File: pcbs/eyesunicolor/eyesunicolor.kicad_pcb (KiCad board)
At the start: 2 copper layers, 209.3 x 100.6 mm, 45 parts, among them J1 SUPP28, J2 SUPP28, P1 CONN_5X2, P2 CONN_5X2, P3 CONN_5X2

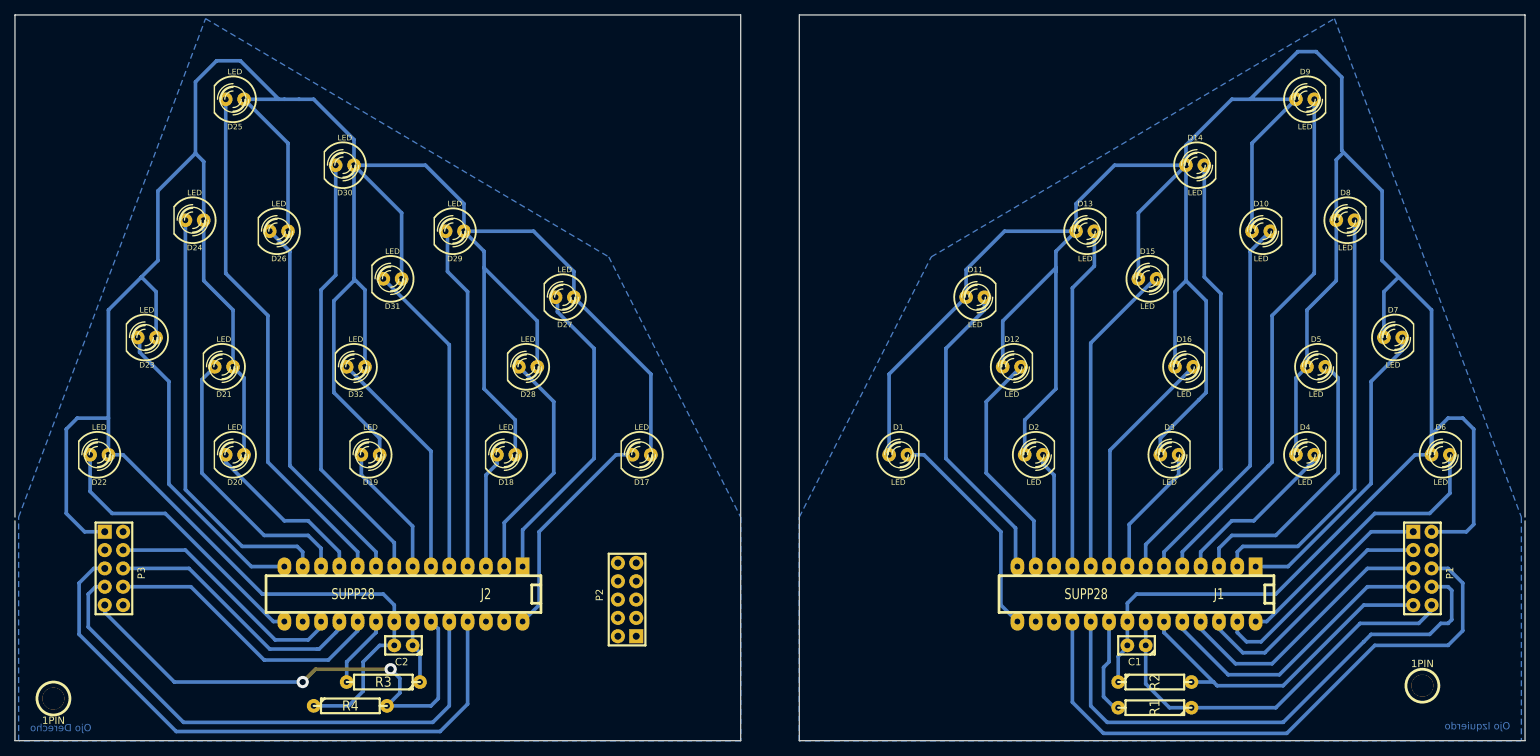
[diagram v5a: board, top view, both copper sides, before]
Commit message: Elimino archivos de backup y actualizo pcb y schm
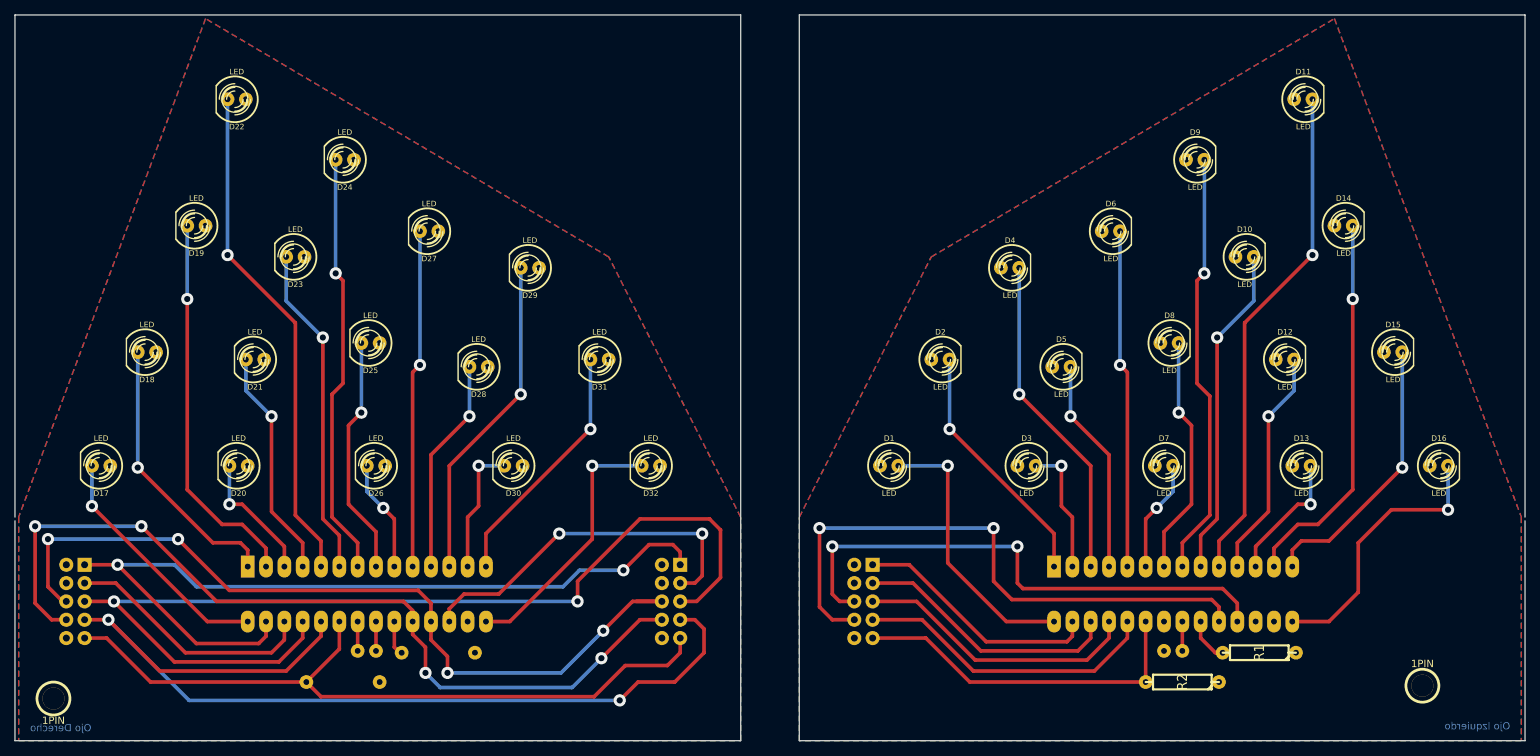
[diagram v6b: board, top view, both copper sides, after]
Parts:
- C1, C2: value C -> 100n; moved to B.Cu
- J1, J2, P1, P2, P3, R3, R4: moved to B.Cu
- moved P1 77.6 mm to (297.4, 109.7)
- moved P3 77.4 mm to (270.8, 109.7)
- moved P2 76.5 mm to (188.2, 109.7), turned to 270 degrees
- moved D17 74.9 mm to (191.8, 90.9)
- moved D6 55.2 mm to (331.7, 58.4)
- moved D11 53.1 mm to (358.4, 40.1)
- moved D22 52.8 mm to (210.6, 40.1)
- moved D18 51.8 mm to (198.1, 75.2)
- moved D4 48.4 mm to (317.8, 63.5)
- moved D30 47.8 mm to (248.9, 90.9)
- moved D13 44.2 mm to (358.1, 90.9)
- moved D32 43.1 mm to (268.0, 90.9)
- moved D19 39.9 mm to (205.0, 57.7)
- moved D25 38.7 mm to (229.1, 73.9)
- moved D16 37.9 mm to (377.2, 90.9)
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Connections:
- D1 pad 2: N-0000026 -> N-0000023
- D10 pad 2: N-0000037 -> N-0000035
- D14 pad 2: N-0000036 -> N-0000033
- D15 pad 2: N-0000025 -> N-0000026
- D19 pad 2: N-0000056 -> N-0000057
- D2 pad 2: N-0000033 -> N-0000040
- D22 pad 2: N-0000055 -> N-0000056
- D24 pad 2: N-0000057 -> N-0000052
- D25 pad 2: N-0000054 -> N-0000055
- D3 pad 2: N-0000035 -> N-0000039
- D5 pad 2: N-0000039 -> N-0000038
- D7 pad 2: N-0000040 -> N-0000037
- D9 pad 2: N-0000038 -> N-0000036
- J1 pad 10: N-0000025 -> N-0000027
- J1 pad 11: N-0000034 -> N-0000032
- J1 pad 12: N-0000033 -> N-0000034
- J1 pad 13: N-0000032 -> N-0000033
- J1 pad 14: N-0000027 -> N-0000026
- J1 pad 15: N-0000026 -> N-0000028
- J1 pad 16: (no net) -> N-0000025
- J1 pad 17: (no net) -> N-0000024
- J1 pad 2: N-0000030 -> N-0000039
- J1 pad 28: N-0000031 -> N-0000023
- J1 pad 3: N-0000039 -> N-0000029
- J1 pad 4: N-0000029 -> N-0000038
- J1 pad 5: N-0000038 -> N-0000031
- J1 pad 7: N-0000036 -> N-0000030
- J1 pad 8: N-0000035 -> N-0000036
- J1 pad 9: N-0000028 -> N-0000035
- J2 pad 1: N-0000046 -> N-0000047
- J2 pad 10: N-0000054 -> N-0000046
- J2 pad 11: N-0000050 -> N-0000044
- J2 pad 12: N-0000051 -> N-0000043
- J2 pad 13: N-0000057 -> N-0000014
- J2 pad 14: N-0000041 -> N-0000049
- J2 pad 15: N-0000055 -> N-0000048
- J2 pad 16: (no net) -> N-0000054
- J2 pad 2: N-0000044 -> N-0000057
- J2 pad 3: N-0000047 -> N-0000050
- J2 pad 4: N-0000043 -> N-0000051
- J2 pad 5: N-0000049 -> N-0000056
- J2 pad 6: N-0000048 -> N-0000041
- J2 pad 7: N-0000056 -> N-0000052
- J2 pad 8: N-0000014 -> N-0000055
- P1 pad 4: (no net) -> N-0000015
- P2 pad 2: /SCLK_D -> VCC
- P2 pad 4: (no net) -> N-000004
- P2 pad 5: /GSCLK_D -> /SCLK_D
- P2 pad 6: /XLAT_D -> /GSCLK_D
- P2 pad 7: VCC -> /XLAT_D
- P2 pad 8: /BLANK_D -> /DCPRG_D
- P2 pad 9: /DCPRG_D -> /BLANK_D
- P3 pad 1: VCC -> /VPRG_D
- P3 pad 2: (no net) -> VCC
- P3 pad 3: /VPRG_D -> /SOUT_D
- P3 pad 4: /SOUT_D -> N-0000011
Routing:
- net VCC: track 913.2 -> 8.13 mm
- net /VPRG_D: track 0.00 -> 116.0 mm, vias 0 -> 2
- net /DCPRG_D: track 39.7 -> 120.0 mm, vias 0 -> 4
- net /GSCLK_D: track 36.8 -> 114.7 mm, vias 0 -> 4
- net N-0000054: track 72.3 -> 0.00 mm
- net /XLAT_D: track 75.4 -> 136.8 mm, vias 0 -> 2
- net GND: track 64.8 -> 4.06 mm
- net N-0000052: track 0.00 -> 58.9 mm, vias 0 -> 1
- net /SCLK_D: track 83.9 -> 142.0 mm, vias 0 -> 2
- net N-0000056: track 18.4 -> 70.1 mm, vias 0 -> 1
- net N-0000025: track 43.8 -> 0.00 mm
- net N-0000014: track 60.7 -> 18.2 mm, vias 0 -> 1
- net N-0000038: track 72.3 -> 29.9 mm, vias 0 -> 1
- net N-0000023: track 0.00 -> 38.4 mm, vias 0 -> 1
- net N-0000033: track 16.1 -> 53.4 mm, vias 0 -> 1
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- added copper zone on F.Cu, net GND
- removed copper zone on B.Cu, net GND

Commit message: agrego los bordes y mas agujeros de montaje
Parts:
- added 1PIN: P***, 1pin, F.Cu at (132.3, 148.6)
- added 1PIN: P***, 1pin, F.Cu at (203.2, 185.2)
- added 1PIN: P***, 1pin, F.Cu at (144.0, 113.0)
- added 1PIN: P***, 1pin, F.Cu at (275.8, 113.3)
- added 1PIN: P***, 1pin, F.Cu at (170.2, 132.1)
- added 1PIN: P***, 1pin, F.Cu at (182.4, 148.6)
- added 1PIN: P***, 1pin, F.Cu at (237.5, 148.6)
- added 1PIN: P***, 1pin, F.Cu at (249.7, 132.1)
- added 1PIN: P***, 1pin, F.Cu at (287.5, 148.6)
- added 1PIN: P***, 1pin, F.Cu at (216.7, 185.2)
- moved D10 100.6 mm to (273.3, 126.7)
- moved D14 100.6 mm to (287.0, 122.4)
- moved D1 100.6 mm to (224.0, 155.7)
- moved D3 100.6 mm to (243.1, 155.7)
- moved D4 100.6 mm to (240.8, 128.3)
- moved P1 100.6 mm to (220.5, 174.5)
- moved C1 100.6 mm to (263.4, 181.4)
- moved D11 100.6 mm to (281.4, 104.9)
- moved D12 100.6 mm to (278.9, 141.0)
- moved D13 100.6 mm to (281.2, 155.7)
- moved D15 100.6 mm to (293.9, 140.0)
- moved D16 100.6 mm to (300.2, 155.7)
- moved D2 100.6 mm to (231.1, 141.0)
- moved D5 100.6 mm to (247.9, 142.0)
- moved D6 100.6 mm to (254.8, 123.2)
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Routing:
- net N-0000033: track 53.4 -> 55.9 mm
- net /XLAT_D: track 136.8 -> 134.3 mm
- net N-0000057: track 53.4 -> 55.7 mm
- net /SCLK_D: track 142.0 -> 141.0 mm
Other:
- board size 209.3 x 100.6 mm -> 203.5 x 96.5 mm

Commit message: cambio la hoja a A4 y agrego rotulo
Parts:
- moved C1 71.4 mm to (204.0, 141.7)
- moved D9 71.4 mm to (207.0, 73.7)
- moved J1 71.4 mm to (204.0, 133.9)
- moved 1PIN 71.4 mm to (72.9, 109.0)
- moved 1PIN 71.4 mm to (216.4, 73.7)
- moved 1PIN 71.4 mm to (110.7, 92.5)
- moved 1PIN 71.4 mm to (122.9, 109.0)
- moved 1PIN 71.4 mm to (178.1, 109.0)
- moved 1PIN 71.4 mm to (228.1, 109.0)
- moved D4 71.4 mm to (181.4, 88.6)
- moved R1 71.4 mm to (215.9, 142.0)
- moved R3 71.4 mm to (106.9, 142.0)
- moved 1PIN 71.4 mm to (53.8, 145.5)
- moved 1PIN 71.4 mm to (84.6, 73.4)
- moved 1PIN 71.4 mm to (157.2, 145.5)
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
